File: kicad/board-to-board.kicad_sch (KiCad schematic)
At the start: 2 parts, among them J8 DF40TC-50DP-0.4V(51), J9 DF40TC-50DP-0.4V(51)

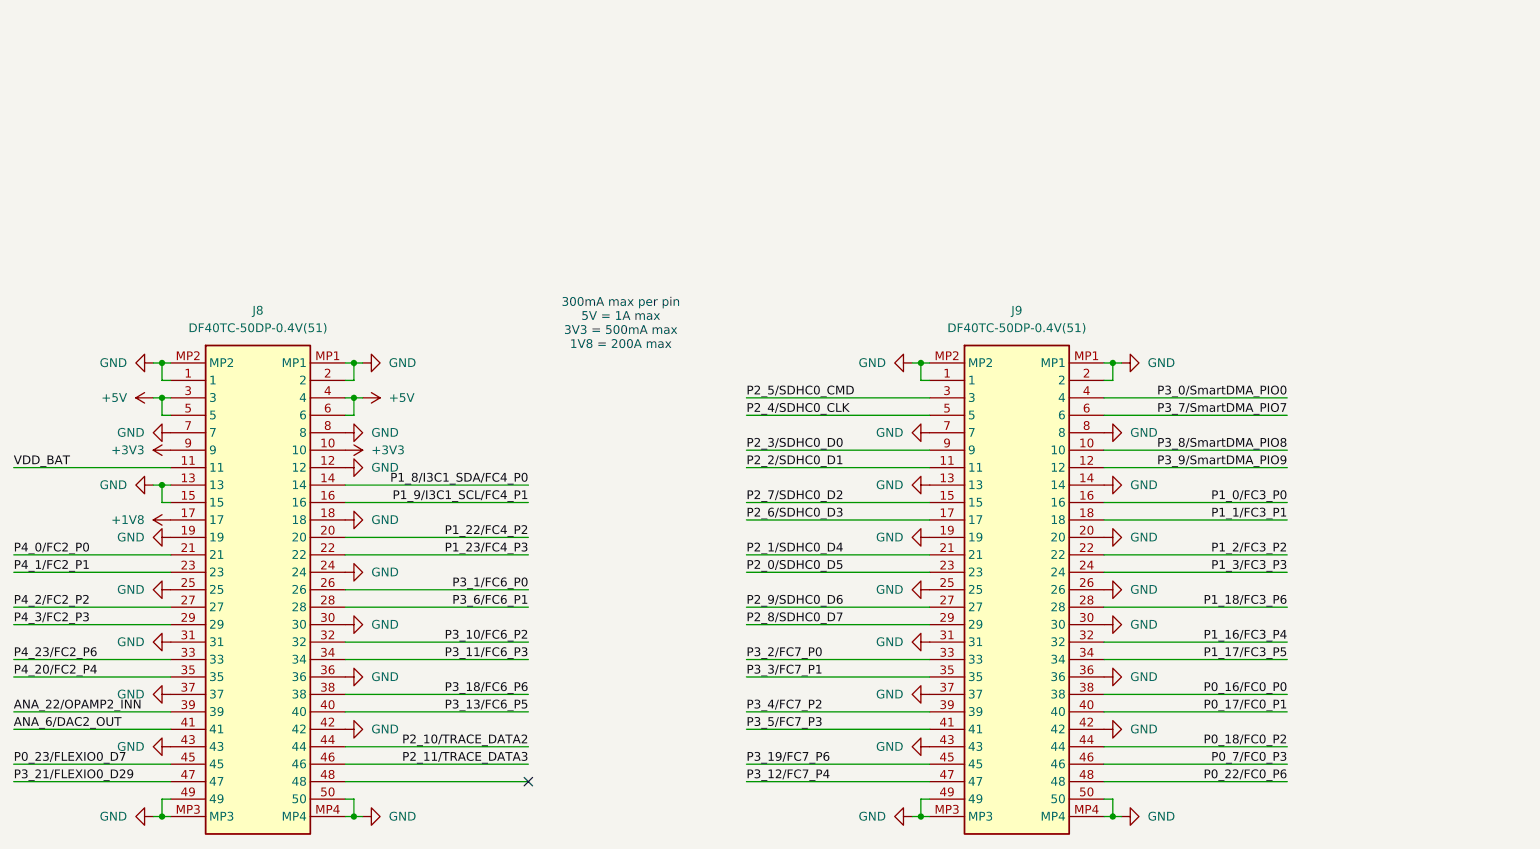
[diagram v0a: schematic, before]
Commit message: Updated schematic and started on layout
- Implemented schematic changes after feedback:
	- BMM350 VDD is 1.8V
	- Replaced net labels with global labels for page references
	- Added 1uF cap to SK9822-EC20
- Added rev-RMII configuration for TJA1103 and DNP resistor to put it in slave mode
- Added TJA1103 PHY address info
- Changed decoupling caps for MCXN to smallest possible packages
- Added traces and vias at MCXN according to guidelines
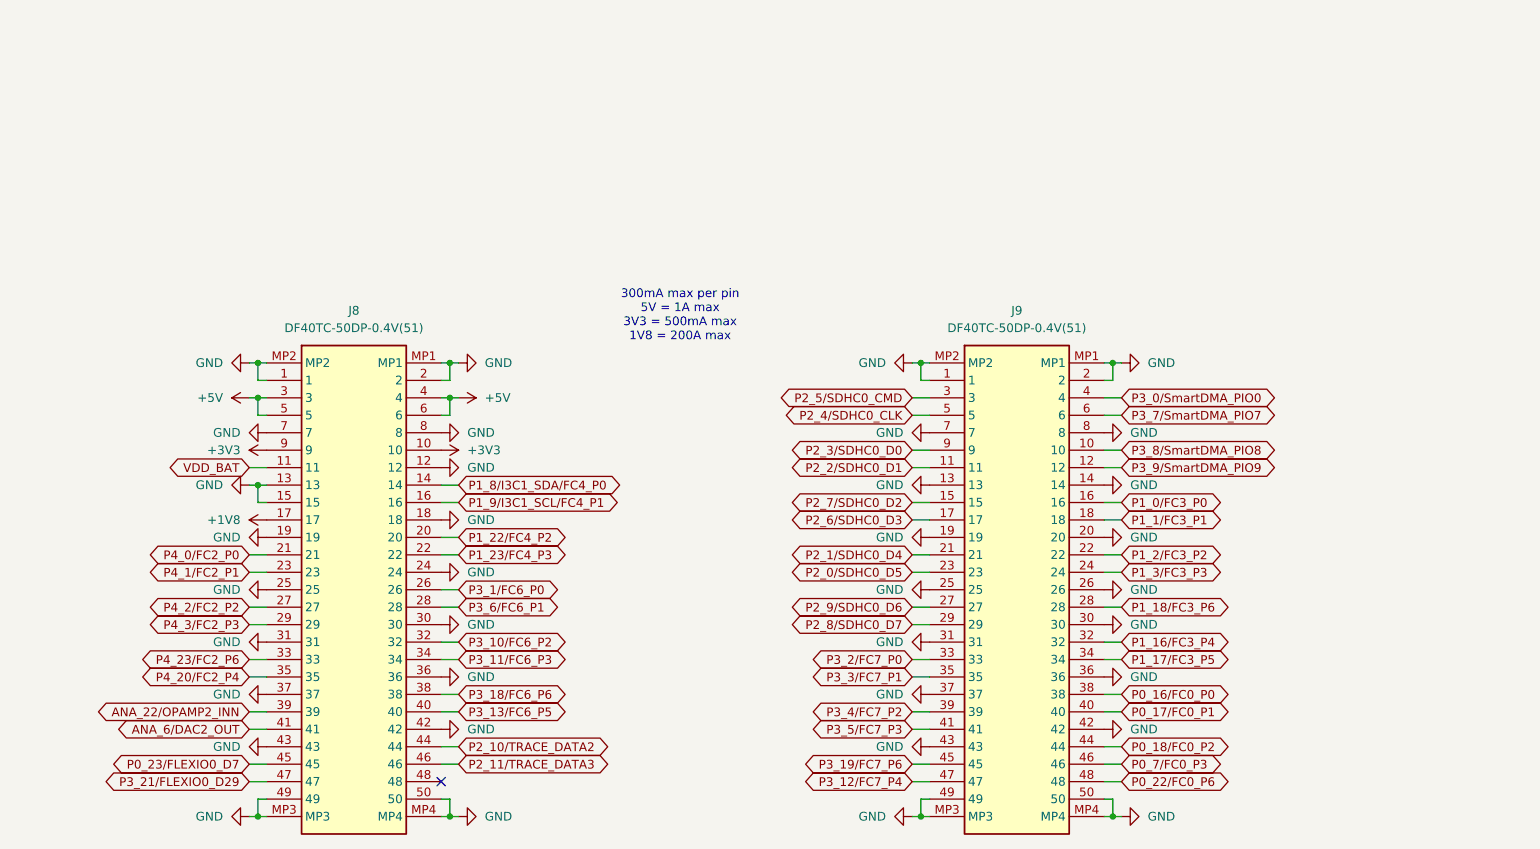
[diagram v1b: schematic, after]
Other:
- moved on the sheet: J8

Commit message: Updated schematic after feedback from Jari
- Finished schematic after feedback from Jari. It is at a finished state, can be reviewed by whole team now.
- Layouted MCXN with decoupling caps.
- Layouted Base100-T1 ethernet phy.
- Layouted the power supply a bit.
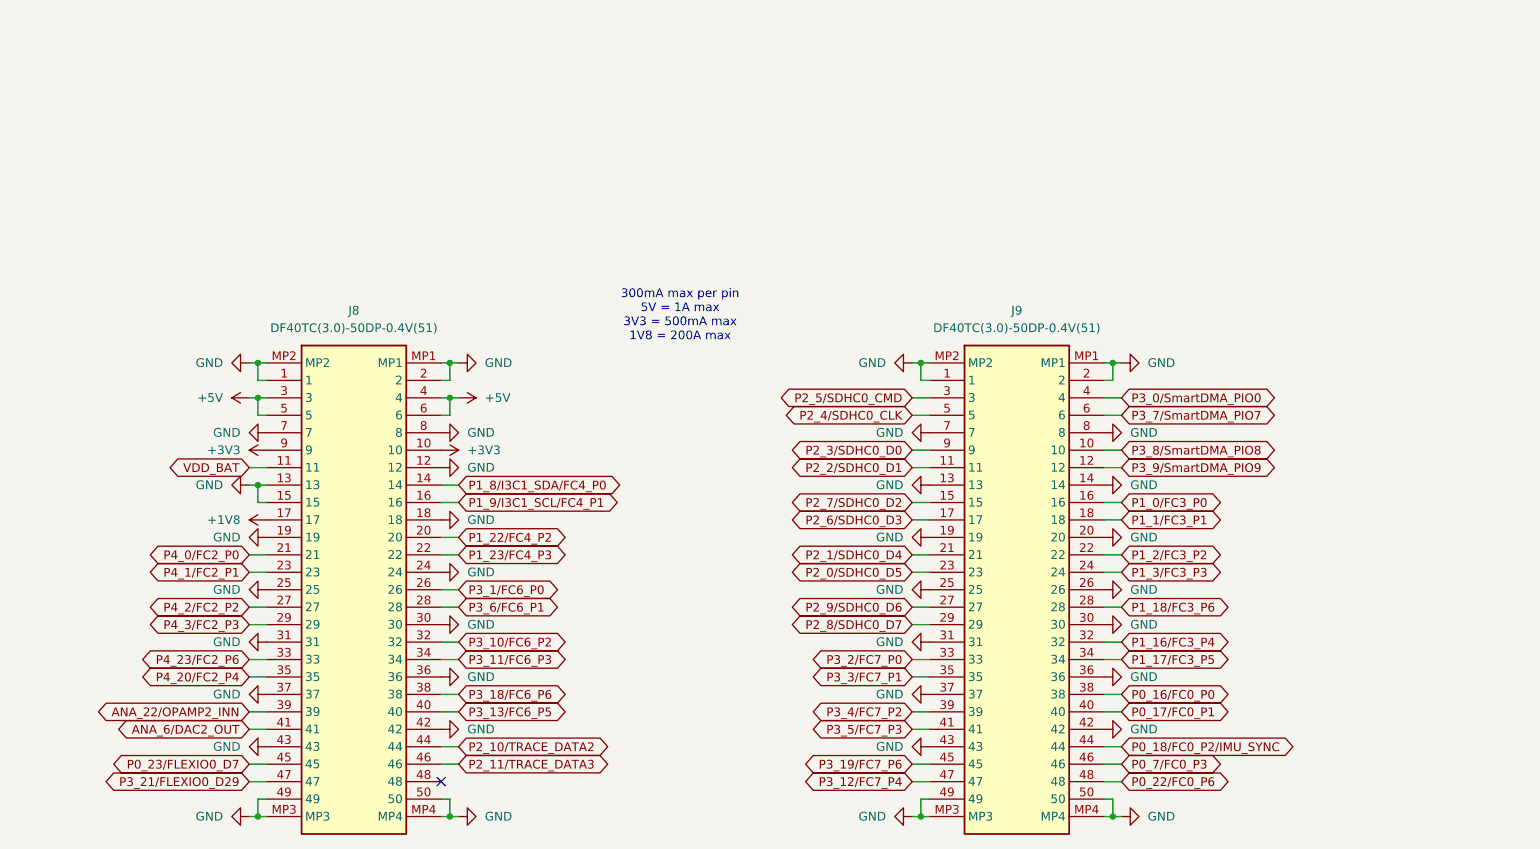
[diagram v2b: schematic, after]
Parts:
- J8, J9: value DF40TC-50DP-0.4V(51) -> DF40TC(3.0)-50DP-0.4V(51); footprint Connectors:DF40TC-50DP-0.4V(51) -> Connectors:DF40TC(3.0)-50DP-0.4V(51); symbol Connectors:DF40TC-50DP-0.4V(51) -> Connectors:DF40TC(3.0)-50DP-0.4V(51); MFPN DF40TC-50DP-0.4V(51) -> DF40TC(3.0)-30DS-0.4V(51); Supplier JLCPCB -> Farnell; Supplier PN C3648702 -> 4399391
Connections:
- net P0_18/FC0_P2 renamed P0_18/FC0_P2/IMU_SYNC
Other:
- title: MR-MCXN-T1 Sensor hub -> MR-MCXN-T1 Sensor Node
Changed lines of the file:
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@@
 	(paper "A4")
 	(title_block
-		(title "MR-MCXN-T1 Sensor hub")
-		(date "2025-03-20")
+		(title "MR-MCXN-T1 Sensor Node")
+		(date "2025-03-28")
 		(rev "X0")
 		(company "NXP SEMICONDUCTORS B.V.")
@@
 		)
 	)
+	(global_label "P0_18{slash}FC0_P2{slash}IMU_SYNC"
+		(shape bidirectional)
+		(at 217.17 123.19 0)
+		(fields_autoplaced yes)
+		(effects
+			(font
+				(size 1.27 1.27)
+			)
+			(justify left)
+		)
+		(property "Intersheetrefs" "${INTERSHEET_REFS}"
+			(at 246.0617 123.19 0)
+			(effects
+				(font
+					(size 1.27 1.27)
+				)
+				(justify left)
+			)
+		)
+	)
 	(global_label "P3_12{slash}FC7_P4"
 		(shape bidirectional)
@@
 		)
 	)
-	(global_label "P0_18{slash}FC0_P2"
-		(shape bidirectional)
-		(at 217.17 123.19 0)
-		(fields_autoplaced yes)
-		(effects
-			(font
-				(size 1.27 1.27)
-			)
-			(justify left)
-		)
-		(property "Intersheetrefs" "${INTERSHEET_REFS}"
-			(at 235.4783 123.19 0)
-			(effects
-				(font
-					(size 1.27 1.27)
-				)
-				(justify left)
-			)
-		)
-	)
 	(global_label "P1_18{slash}FC3_P6"
 		(shape bidirectional)
@@
 	)
 	(symbol
-		(lib_id "Connectors:DF40TC-50DP-0.4V(51)")
+		(lib_id "Connectors:DF40TC(3.0)-50DP-0.4V(51)")
 		(at 92.71 67.31 0)
 		(unit 1)
@@
 			)
 		)
-		(property "Value" "DF40TC-50DP-0.4V(51)"
+		(property "Value" "DF40TC(3.0)-50DP-0.4V(51)"
 			(at 105.41 62.23 0)
 			(effects
@@
 			)
 		)
-		(property "Footprint" "Connectors:DF40TC-50DP-0.4V(51)"
+		(property "Footprint" "Connectors:DF40TC(3.0)-50DP-0.4V(51)"
 			(at 105.918 137.668 0)
 			(effects
@@
 			)
 		)
-		(property "Supplier" "JLCPCB"
+		(property "Supplier" "Farnell"
 			(at 92.71 67.31 0)
 			(effects
@@
 			)
 		)
-		(property "MFPN" "DF40TC-50DP-0.4V(51)"
-			(at 92.71 67.31 0)
-			(effects
-				(font
-					(size 1.27 1.27)
-				)
-				(hide yes)
-			)
-		)
-		(property "Supplier PN" "C3648702"
-			(at 92.71 67.31 0)
-			(effects
-				(font
-					(size 1.27 1.27)
-				)
-				(hide yes)
-			)
-		)
-		(property "MANUFACTURER" ""
-			(at 92.71 67.31 0)
-			(effects
-				(font
-					(size 1.27 1.27)
-				)
-				(hide yes)
-			)
-		)
-		(property "MAXIMUM_PACKAGE_HEIGHT" ""
-			(at 92.71 67.31 0)
-			(effects
-				(font
-					(size 1.27 1.27)
-				)
-				(hide yes)
-			)
-		)
-		(property "PARTREV" ""
+		(property "MFPN" "DF40TC(3.0)-30DS-0.4V(51)"
 			(at 92.71 67.31 0)
 			(effects
@@
 			)
 		)
-		(property "STANDARD" ""
+		(property "Supplier PN" "4399391"
 			(at 92.71 67.31 0)
 			(effects
@@
 	)
 	(symbol
-		(lib_id "Connectors:DF40TC-50DP-0.4V(51)")
+		(lib_id "Connectors:DF40TC(3.0)-50DP-0.4V(51)")
 		(at 189.23 67.31 0)
 		(unit 1)
@@
 			)
 		)
-		(property "Value" "DF40TC-50DP-0.4V(51)"
+		(property "Value" "DF40TC(3.0)-50DP-0.4V(51)"
 			(at 201.93 62.23 0)
 			(effects
@@
 			)
 		)
-		(property "Footprint" "Connectors:DF40TC-50DP-0.4V(51)"
+		(property "Footprint" "Connectors:DF40TC(3.0)-50DP-0.4V(51)"
 			(at 202.438 137.668 0)
 			(effects
@@
 			)
 		)
-		(property "Supplier" "JLCPCB"
+		(property "Supplier" "Farnell"
 			(at 189.23 67.31 0)
 			(effects
@@
 			)
 		)
-		(property "MFPN" "DF40TC-50DP-0.4V(51)"
+		(property "MFPN" "DF40TC(3.0)-30DS-0.4V(51)"
 			(at 189.23 67.31 0)
 			(effects
@@
 			)
 		)
-		(property "Supplier PN" "C3648702"
+		(property "Supplier PN" "4399391"
 			(at 189.23 67.31 0)
 			(effects

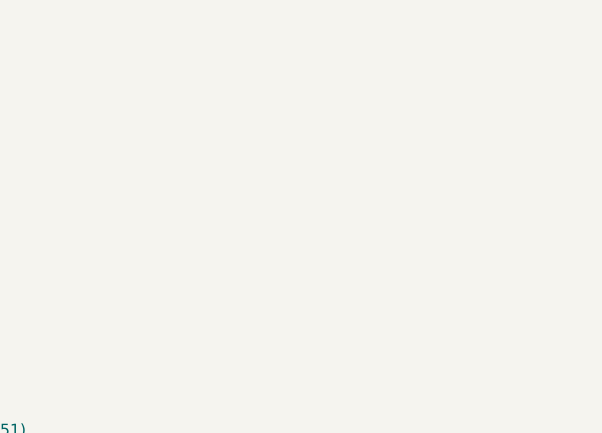
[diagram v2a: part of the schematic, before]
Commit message: Finished schematic. Completed power and ENET phy layout.
Layouted power supply and ethernet phy around input connector.
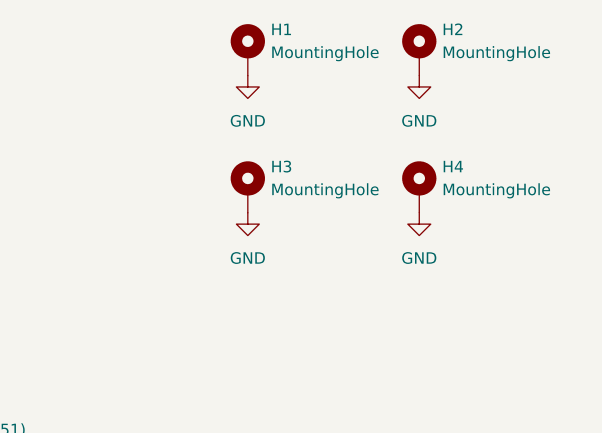
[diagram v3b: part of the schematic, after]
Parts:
- added H1, H2, H3, H4: MountingHole, MountingHole:MountingHole_3.2mm_M3_DIN965_Pad, symbol Mechanical:MountingHole_Pad
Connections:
- net GND: now also H1.1, H2.1, H3.1, H4.1

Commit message: Updated layout and BOM
- Rounded corners of PCB
- Updated board-to-board MFPN to correct one.
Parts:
- J8, J9: MFPN DF40TC(3.0)-30DS-0.4V(51) -> DF40TC(3.0)-50DP-0.4V(51); Supplier Farnell -> Mouser; Supplier PN 4399391 -> 798-DF40TC3050DP04V5
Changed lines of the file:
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@@
 			)
 		)
-		(property "Supplier" "Farnell"
+		(property "Supplier" "Mouser"
 			(at 92.71 67.31 0)
 			(effects
@@
 			)
 		)
-		(property "MFPN" "DF40TC(3.0)-30DS-0.4V(51)"
+		(property "MFPN" "DF40TC(3.0)-50DP-0.4V(51)"
 			(at 92.71 67.31 0)
 			(effects
@@
 			)
 		)
-		(property "Supplier PN" "4399391"
+		(property "Supplier PN" "798-DF40TC3050DP04V5"
 			(at 92.71 67.31 0)
 			(effects
@@
 			)
 		)
-		(property "Supplier" "Farnell"
+		(property "Supplier" "Mouser"
 			(at 189.23 67.31 0)
 			(effects
@@
 			)
 		)
-		(property "MFPN" "DF40TC(3.0)-30DS-0.4V(51)"
+		(property "MFPN" "DF40TC(3.0)-50DP-0.4V(51)"
 			(at 189.23 67.31 0)
 			(effects
@@
 			)
 		)
-		(property "Supplier PN" "4399391"
+		(property "Supplier PN" "798-DF40TC3050DP04V5"
 			(at 189.23 67.31 0)
 			(effects

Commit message: Updated layout and BOM
- Flipped Magnetometer so it is aligned with the axis of the IMU.
- Updated BOM so all parts can be sourced from DigiKey. Also added a row for JLCPCB part numbers if applicable.
- Replaced ISP button with the NanoT160AS. Added "ISP" in silkscreen at that button.
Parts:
- J8, J9: DigiKey (none) -> 26-DF40TC(3.0)-50DP-0.4V(51)CT-ND; JLCPCB (none) -> -; Supplier Mouser -> (none); Supplier PN 798-DF40TC3050DP04V5 -> (none)
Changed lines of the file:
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@@
-			)
-		)
-		(property "Supplier" "Mouser"
-			(at 92.71 67.31 0)
-			(effects
-				(font
-					(size 1.27 1.27)
-				)
-				(hide yes)
 			)
 		)
@@
 			)
 		)
-		(property "Supplier PN" "798-DF40TC3050DP04V5"
+		(property "DigiKey" "26-DF40TC(3.0)-50DP-0.4V(51)CT-ND"
+			(at 92.71 67.31 0)
+			(effects
+				(font
+					(size 1.27 1.27)
+				)
+				(hide yes)
+			)
+		)
+		(property "JLCPCB" "-"
 			(at 92.71 67.31 0)
 			(effects
@@
 			)
 		)
-		(property "Supplier" "Mouser"
-			(at 189.23 67.31 0)
-			(effects
-				(font
-					(size 1.27 1.27)
-				)
-				(hide yes)
-			)
-		)
 		(property "MF" "HRS(Hirose)"
 			(at 189.23 67.31 0)
@@
 			)
 		)
-		(property "Supplier PN" "798-DF40TC3050DP04V5"
+		(property "DigiKey" "26-DF40TC(3.0)-50DP-0.4V(51)CT-ND"
 			(at 189.23 67.31 0)
 			(effects
@@
 			)
 		)
-		(property "MANUFACTURER" ""
+		(property "JLCPCB" "-"
 			(at 189.23 67.31 0)
 			(effects
-				(font
-					(size 1.27 1.27)
-				)
-				(hide yes)
-			)
-		)
-		(property "MAXIMUM_PACKAGE_HEIGHT" ""
-			(at 189.23 67.31 0)
-			(effects
-				(font
-					(size 1.27 1.27)
-				)
-				(hide yes)
-			)
-		)
-		(property "PARTREV" ""
-			(at 189.23 67.31 0)
-			(effects
-				(font
-					(size 1.27 1.27)
-				)
-				(hide yes)
-			)
-		)
-		(property "STANDARD" ""
-			(at 189.23 67.31 0)
-			(effects
